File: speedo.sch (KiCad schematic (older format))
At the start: 50 parts, among them J1 Conn_01x08, J2 Conn_01x10, J3 Prog Header, Q1 BSS138, SW1 SW_Push, U1 US1881, U2 LT1762-3.3, U3 4N25, U4 LT1762-5, U5 ATMEGA328P-AU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

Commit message: Moved some pins around
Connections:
- net BUTTON1: now also U5.1 ((PCINT19/OC2B/INT1)PD3); no longer U5.32 ((PCINT18/INT0)PD2)
- net BUTTON2: now also U5.2 ((PCINT20/XCK/T0)PD4); no longer U5.1 ((PCINT19/OC2B/INT1)PD3)
- net HALL-EFF: now also U5.32 ((PCINT18/INT0)PD2); no longer U5.9 ((PCINT21/OC0B/T1)PD5)
- net TACH: now also U5.12 ((PCINT0/CLKO/ICP1)PB0); no longer U5.2 ((PCINT20/XCK/T0)PD4)
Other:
- note added: "PB1 & PB2 unusable for analogWrite"
- moved on the sheet: R9
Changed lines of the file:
@@
 Text GLabel 7750 5350 2    60   Input ~ 0
 LCD-RST
-Text GLabel 8400 3250 2    60   Input ~ 0
+Text GLabel 8550 3250 2    60   Input ~ 0
 LCD-CS
 Text GLabel 7750 5250 2    60   Input ~ 0
@@
 Text GLabel 7750 3900 2    60   Input ~ 0
 VMEAS
-Text GLabel 7750 5150 2    60   Input ~ 0
+Text GLabel 7750 4850 2    60   Input ~ 0
 HALL-EFF
-Text GLabel 7750 5050 2    60   Input ~ 0
+Text GLabel 7700 3050 2    60   Input ~ 0
 TACH
-Text GLabel 7750 4850 2    60   Input ~ 0
+Text GLabel 7750 4950 2    60   Input ~ 0
 BUTTON1
 $Comp
@@
 L R R9
 U 1 1 5B3D0842
-P 8200 3100
-F 0 "R9" V 8280 3100 50  0000 C CNN
-F 1 "10K" V 8200 3100 50  0000 C CNN
-F 2 "Resistors_SMD:R_0603" V 8130 3100 50  0001 C CNN
-F 3 "" H 8200 3100 50  0001 C CNN
-	1    8200 3100
+P 8350 3100
+F 0 "R9" V 8430 3100 50  0000 C CNN
+F 1 "10K" V 8350 3100 50  0000 C CNN
+F 2 "Resistors_SMD:R_0603" V 8280 3100 50  0001 C CNN
+F 3 "" H 8350 3100 50  0001 C CNN
+	1    8350 3100
 	-1   0    0    -1
 $EndComp
@@
 L +3.3V #PWR039
 U 1 1 5B3D0C7B
-P 8200 2950
-F 0 "#PWR039" H 8200 2800 50  0001 C CNN
-F 1 "+3.3V" H 8200 3090 50  0000 C CNN
-F 2 "" H 8200 2950 50  0001 C CNN
-F 3 "" H 8200 2950 50  0001 C CNN
-	1    8200 2950
+P 8350 2950
+F 0 "#PWR039" H 8350 2800 50  0001 C CNN
+F 1 "+3.3V" H 8350 3090 50  0000 C CNN
+F 2 "" H 8350 2950 50  0001 C CNN
+F 3 "" H 8350 2950 50  0001 C CNN
+	1    8350 2950
 	1    0    0    -1
 $EndComp
@@
 Text GLabel 4100 1200 0    60   Input ~ 0
 BUTTON2
-Text GLabel 7750 4950 2    60   Input ~ 0
+Text GLabel 7750 5050 2    60   Input ~ 0
 BUTTON2
 $Comp
@@
 	7500 3550 7750 3550
 Connection ~ 5000 3900
-Connection ~ 8200 3250
+Connection ~ 8350 3250
 Wire Wire Line
 	7500 4650 7650 4650
@@
 Wire Wire Line
 	8250 4750 8400 4750
-Wire Wire Line
-	7750 5150 7500 5150
 Wire Wire Line
 	7500 5250 7750 5250
@@
 	7500 4500 7750 4500
 Wire Wire Line
-	7500 3250 8400 3250
+	7500 3250 8550 3250
 Wire Wire Line
 	7500 5050 7750 5050
@@
 	1    0    0    -1
 $EndComp
-NoConn ~ 7500 3050
 NoConn ~ 7500 3150
 NoConn ~ 7500 4300
@@
 NoConn ~ 5600 4400
 NoConn ~ 5600 4500
+Wire Wire Line
+	7500 3050 7700 3050
+NoConn ~ 7500 5150
+Text Notes 8200 3500 0    60   ~ 0
+PB1 & PB2 unusable for analogWrite
 $EndSCHEMATC

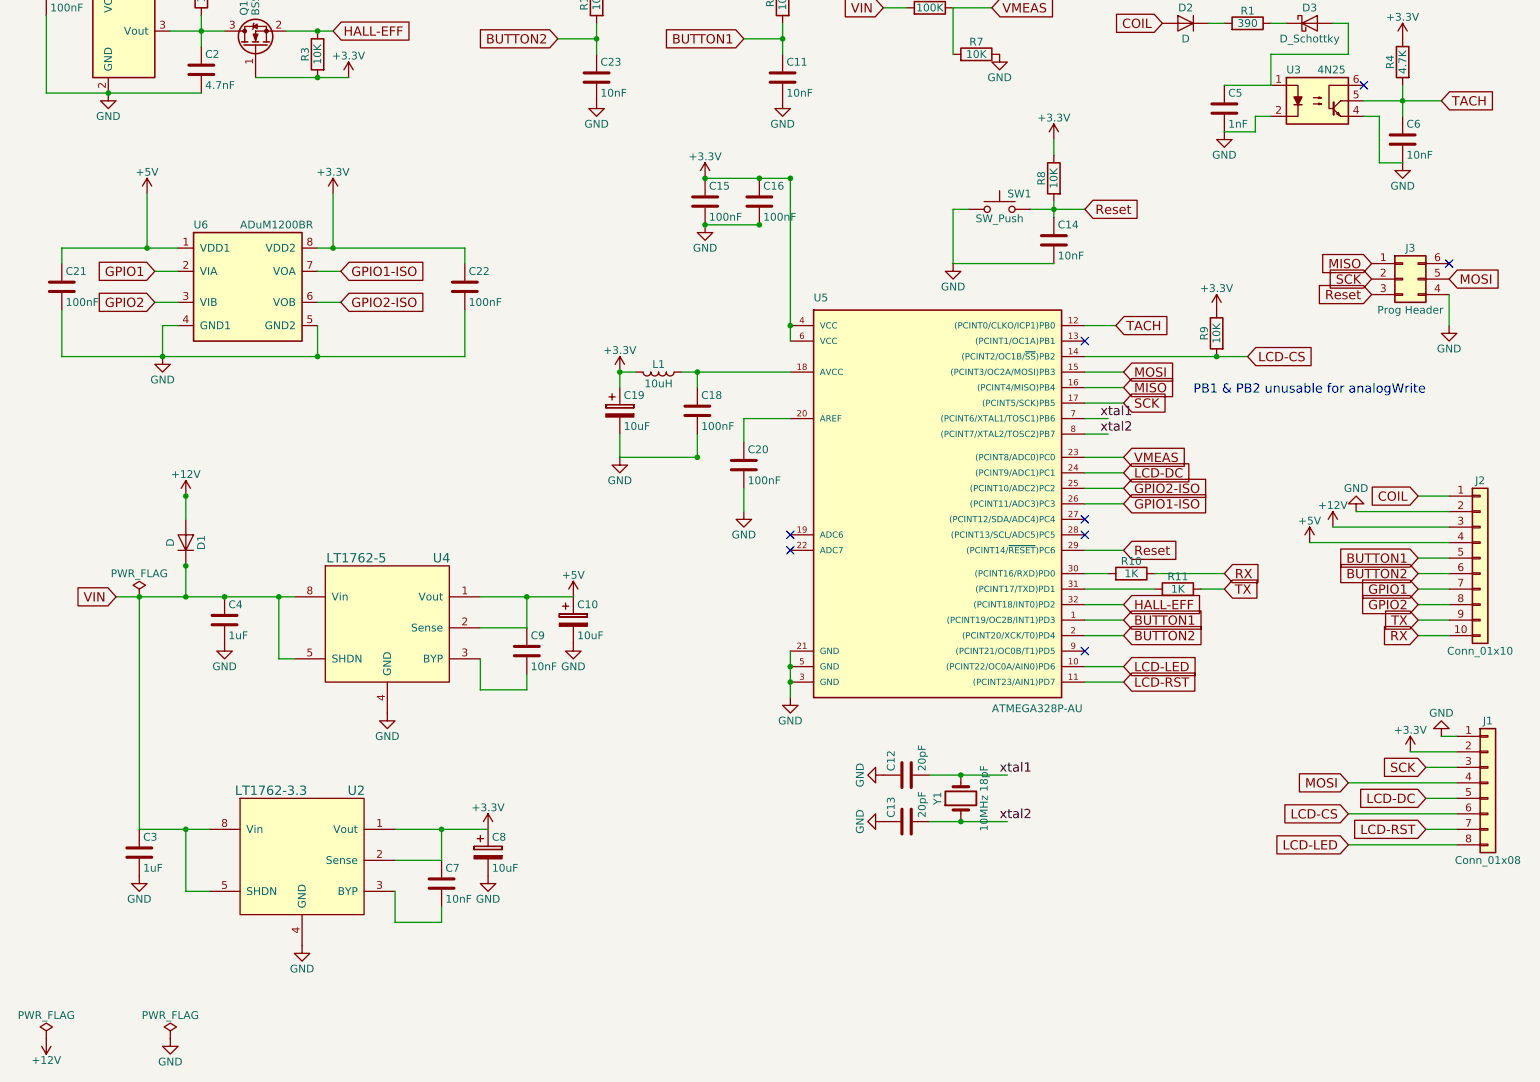
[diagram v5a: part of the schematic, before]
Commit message: Merged atmega644
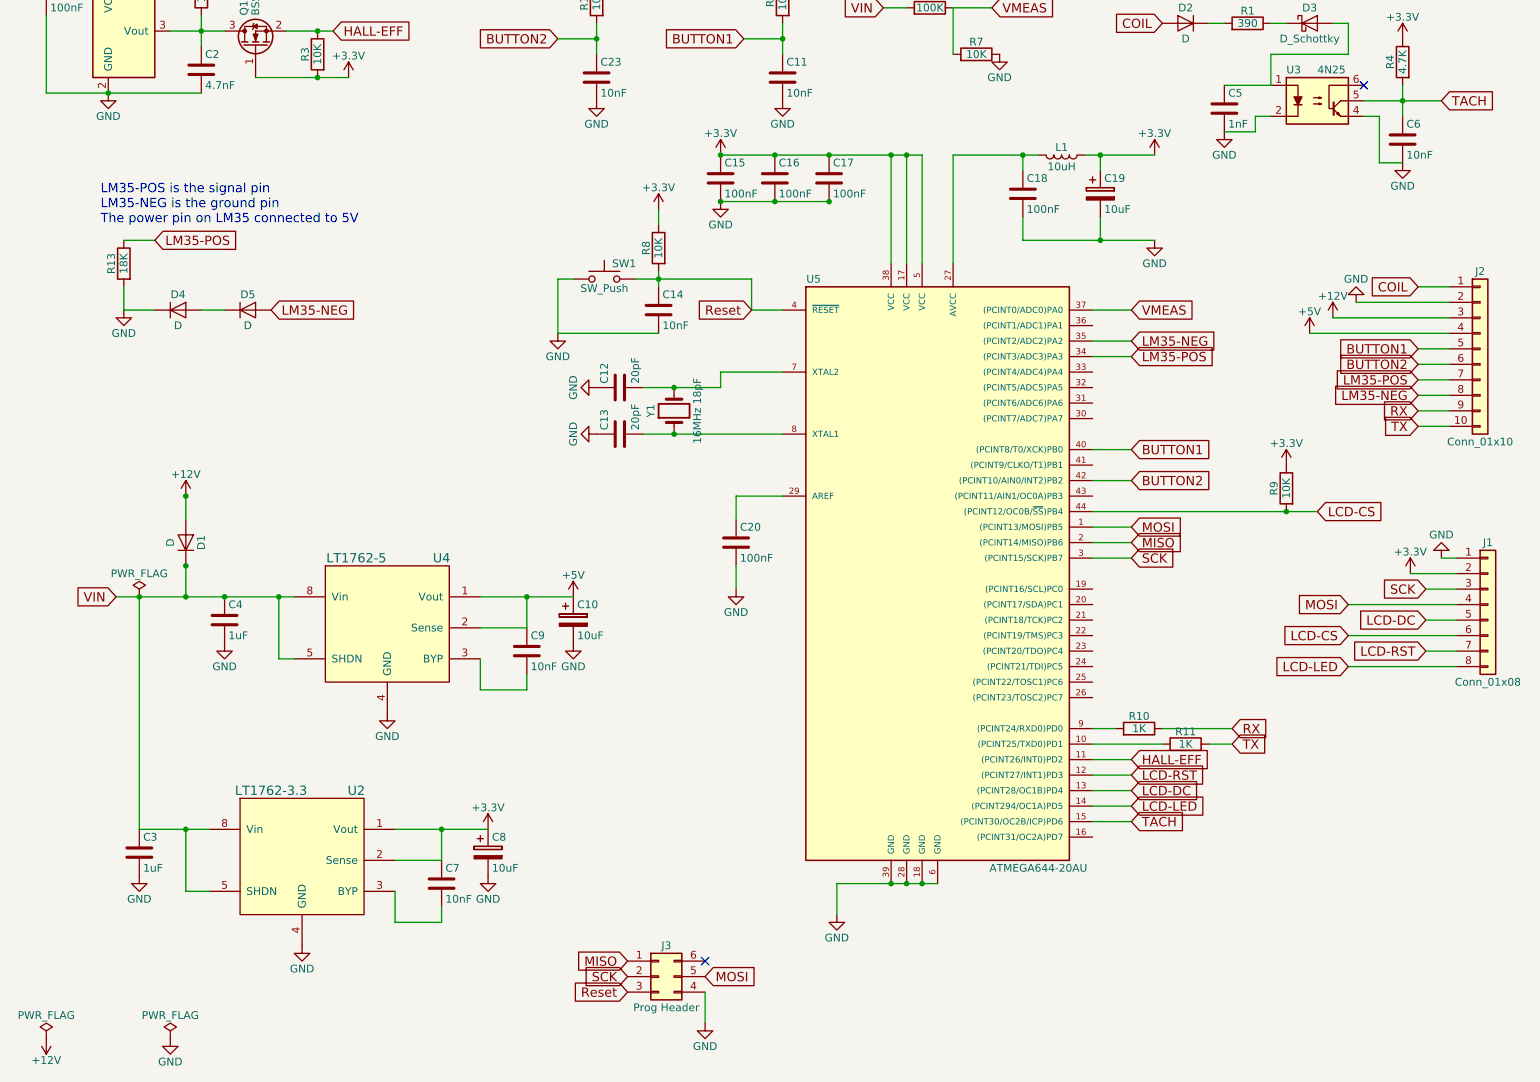
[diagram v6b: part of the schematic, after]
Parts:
- removed C21, C22: 100nF, Capacitors_SMD:C_0603, symbol C
- removed U5: ATMEGA328P-AU, Housings_QFP:TQFP-32_7x7mm_Pitch0.8mm, symbol ATMEGA328P-AU
- removed U6: ADuM1200BR, Housings_SOIC:SOIC-8_3.9x4.9mm_Pitch1.27mm, symbol ADuM1200BR
- added C17: 100nF, Capacitors_SMD:C_0603, symbol C
- added D4, D5: D, Diodes_SMD:D_SOD-123F, symbol D
- added R13: 18K, Resistors_SMD:R_0603, symbol R
- added U5: ATMEGA644-20AU, Housings_QFP:TQFP-44_10x10mm_Pitch0.8mm, symbol ATMEGA644-20AU
- Y1: value 10MHz 18pF -> 16MHz 18pF
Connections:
- net +3V3: now also L1.1, C17.1, U5.17 (VCC), U5.38 (VCC), U5.5 (VCC); no longer L1.2
- net BUTTON1: now also U5.40 ((PCINT8/T0/XCK)PB0)
- net BUTTON2: now also U5.42 ((PCINT10/AIN0/INT2)PB2)
- net GND: now also C17.2, D4.1 (K), R13.2, U5.18 (GND), U5.28 (GND), U5.39 (GND), U5.6 (GND)
- net HALL-EFF: now also U5.11 ((PCINT26/INT0)PD2)
- net LCD-CS: now also U5.44 ((PCINT12/OC0B/~SS~)PB4)
- net LCD-DC: now also U5.13 ((PCINT28/OC1B)PD4)
- net LCD-LED: now also U5.14 ((PCINT294/OC1A)PD5)
- net LCD-RST: now also U5.12 ((PCINT27/INT1)PD3)
- net MISO: now also U5.2 ((PCINT14/MISO)PB6)
- net MOSI: now also U5.1 ((PCINT13/MOSI)PB5)
- net RX: now also J2.9 (Pin_9); no longer J2.10 (Pin_10)
- net Reset: now also U5.4 (~RESET)
- net SCK: now also U5.3 ((PCINT15/SCK)PB7)
- net TACH: now also U5.15 ((PCINT30/OC2B/ICP)PD6)
- net TX: now also J2.10 (Pin_10); no longer J2.9 (Pin_9)
- net VMEAS: now also U5.37 ((PCINT0/ADC0)PA0)
- net at C18.1: now also L1.2, U5.27 (AVCC); no longer L1.1
- net at R10.2: now also U5.9 ((PCINT24/RXD0)PD0)
- net at R11.2: now also U5.10 ((PCINT25/TXD0)PD1)
- net at C20.1: now also U5.29 (AREF)
- net GPIO1 renamed LM35-POS
- net LM35-POS: now also R13.1, U5.34 ((PCINT3/ADC3)PA3)
- net GPIO2 renamed LM35-NEG
- net LM35-NEG: now also D5.2 (A), U5.35 ((PCINT2/ADC2)PA2)
- net xtal1: no longer names the net of C12.2, Y1.2
- net xtal1: now also U5.7 (XTAL2)
- net xtal2: no longer names the net of C13.2, Y1.1
- net xtal2: now also U5.8 (XTAL1)
- new net: D4.2 (A), D5.1 (K)
- no-connect marks 8 -> 2
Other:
- note added: "LM35-POS is the signal pin\nLM35-NEG is the ground pin\nThe power pin on LM35 connected to 5V"
- note removed: "PB1 & PB2 unusable for analogWrite"
- moved on the sheet: C12, C13, C14, C15, C16, C18, C19, C20, J1, J2, J3, L1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

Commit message: Fixed ISP programmer and traces
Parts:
- removed J3: Prog Header, Pin_Headers:Pin_Header_Straight_2x03_Pitch2.54mm, symbol Conn_02x03_Counter_Clockwise
- added J3: ISP, symbol Conn_02x03_Odd_Even
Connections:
- net GND: now also J3.6 (Pin_6)
- net MISO: now also J3.1 (Pin_1)
- net MOSI: now also J3.4 (Pin_4)
- net Reset: now also J3.5 (Pin_5)
- net SCK: now also J3.3 (Pin_3)
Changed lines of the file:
@@
 Title "Speedo"
 Date ""
-Rev ""
+Rev "2.1"
 Comp ""
 Comment1 ""
@@
 Wire Wire Line
 	4100 3100 4750 3100
-$Comp
-L Conn_02x03_Counter_Clockwise J3
-U 1 1 5B3C47E1
-P 4750 7250
-F 0 "J3" H 4800 7450 50  0000 C CNN
-F 1 "Prog Header" H 4800 7050 50  0000 C CNN
-F 2 "Pin_Headers:Pin_Header_Straight_2x03_Pitch2.54mm" H 4750 7250 50  0001 C CNN
-F 3 "" H 4750 7250 50  0001 C CNN
-	1    4750 7250
-	1    0    0    -1
-$EndComp
 Wire Wire Line
 	5050 7350 5050 7550
@@
 Text Notes 1150 2400 0    60   ~ 0
 LM35-POS is the signal pin\nLM35-NEG is the ground pin\nThe power pin on LM35 connected to 5V
+$Comp
+L Conn_02x03_Odd_Even J3
+U 1 1 5BB6DB85
+P 4750 7250
+F 0 "J3" H 4800 7450 50  0000 C CNN
+F 1 "ISP" H 4800 7050 50  0000 C CNN
+F 2 "" H 4750 7250 50  0001 C CNN
+F 3 "" H 4750 7250 50  0001 C CNN
+	1    4750 7250
+	1    0    0    -1
+$EndComp
 $EndSCHEMATC
